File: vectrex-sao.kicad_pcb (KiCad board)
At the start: 2 copper layers, 0 parts

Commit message: initial commit
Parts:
- added C1-1: LED0603_NOOUTLINE, Capacitor_SMD:C_0603_1608Metric, F.Cu at (112.6, 42.4)
- added C1-2: LED0603_NOOUTLINE, Capacitor_SMD:C_0603_1608Metric, F.Cu at (121.6, 49.9)
- added C1-3: LED0603_NOOUTLINE, Capacitor_SMD:C_0603_1608Metric, F.Cu at (91.7, 57.5)
- added C1-4: LED0603_NOOUTLINE, Capacitor_SMD:C_0603_1608Metric, F.Cu at (100.6, 34.9)
- added C1-5: LED0603_NOOUTLINE, Capacitor_SMD:C_0603_1608Metric, F.Cu at (103.7, 57.4)
- added C1-6: LED0603_NOOUTLINE, Capacitor_SMD:C_0603_1608Metric, F.Cu at (128.7, 29.8)
- added C1-7: LED0603_NOOUTLINE, Capacitor_SMD:C_0603_1608Metric, F.Cu at (136.7, 29.8)
- added C2-1: LED0603_NOOUTLINE, Capacitor_SMD:C_0603_1608Metric, F.Cu at (100.6, 32.3)
- added C2-2: LED0603_NOOUTLINE, Capacitor_SMD:C_0603_1608Metric, F.Cu at (108.6, 29.8)
- added C2-3: LED0603_NOOUTLINE, Capacitor_SMD:C_0603_1608Metric, F.Cu at (87.7, 57.5)
- added C2-4: LED0603_NOOUTLINE, Capacitor_SMD:C_0603_1608Metric, F.Cu at (112.6, 44.9)
- added C2-5: LED0603_NOOUTLINE, Capacitor_SMD:C_0603_1608Metric, F.Cu at (125.6, 47.4)
- added C2-6: LED0603_NOOUTLINE, Capacitor_SMD:C_0603_1608Metric, F.Cu at (101.6, 47.4)
- added C2-7: LED0603_NOOUTLINE, Capacitor_SMD:C_0603_1608Metric, F.Cu at (108.6, 42.4)
- added C3-1: LED0603_NOOUTLINE, Capacitor_SMD:C_0603_1608Metric, F.Cu at (100.6, 44.9)
- added C3-2: LED0603_NOOUTLINE, Capacitor_SMD:C_0603_1608Metric, F.Cu at (108.6, 34.9)
- added C3-3: LED0603_NOOUTLINE, Capacitor_SMD:C_0603_1608Metric, F.Cu at (104.6, 29.8)
- added C3-4: LED0603_NOOUTLINE, Capacitor_SMD:C_0603_1608Metric, F.Cu at (108.6, 32.3)
- added C3-5: LED0603_NOOUTLINE, Capacitor_SMD:C_0603_1608Metric, F.Cu at (104.6, 34.9)
- added C3-6: LED0603_NOOUTLINE, Capacitor_SMD:C_0603_1608Metric, F.Cu at (120.7, 37.4)
- added C3-7: LED0603_NOOUTLINE, Capacitor_SMD:C_0603_1608Metric, F.Cu at (101.6, 49.9)
- added C4-1: LED0603_NOOUTLINE, Capacitor_SMD:C_0603_1608Metric, F.Cu at (101.6, 52.4)
- added C4-2: LED0603_NOOUTLINE, Capacitor_SMD:C_0603_1608Metric, F.Cu at (112.6, 29.8)
- added C4-3: LED0603_NOOUTLINE, Capacitor_SMD:C_0603_1608Metric, F.Cu at (113.6, 47.4)
- added C4-4: LED0603_NOOUTLINE, Capacitor_SMD:C_0603_1608Metric, F.Cu at (111.8, 57.4)
- added C4-5: LED0603_NOOUTLINE, Capacitor_SMD:C_0603_1608Metric, F.Cu at (124.7, 37.4)
- added C4-6: LED0603_NOOUTLINE, Capacitor_SMD:C_0603_1608Metric, F.Cu at (128.7, 34.9)
- added C4-7: LED0603_NOOUTLINE, Capacitor_SMD:C_0603_1608Metric, F.Cu at (132.7, 34.9)
- added C5-1: LED0603_NOOUTLINE, Capacitor_SMD:C_0603_1608Metric, F.Cu at (121.6, 47.4)
- added C5-2: LED0603_NOOUTLINE, Capacitor_SMD:C_0603_1608Metric, F.Cu at (117.6, 47.4)
- added C5-3: LED0603_NOOUTLINE, Capacitor_SMD:C_0603_1608Metric, F.Cu at (116.7, 29.8)
- added C5-4: LED0603_NOOUTLINE, Capacitor_SMD:C_0603_1608Metric, F.Cu at (136.7, 34.9)
- added C5-5: LED0603_NOOUTLINE, Capacitor_SMD:C_0603_1608Metric, F.Cu at (99.7, 59.3)
- added C5-6: LED0603_NOOUTLINE, Capacitor_SMD:C_0603_1608Metric, F.Cu at (132.7, 37.4)
- added C5-7: LED0603_NOOUTLINE, Capacitor_SMD:C_0603_1608Metric, F.Cu at (109.6, 52.4)
- added C6-1: LED0603_NOOUTLINE, Capacitor_SMD:C_0603_1608Metric, F.Cu at (107.8, 60.0)
- added C6-2: LED0603_NOOUTLINE, Capacitor_SMD:C_0603_1608Metric, F.Cu at (107.8, 57.4)
- added C6-3: LED0603_NOOUTLINE, Capacitor_SMD:C_0603_1608Metric, F.Cu at (109.6, 47.4)
- added C6-4: LED0603_NOOUTLINE, Capacitor_SMD:C_0603_1608Metric, F.Cu at (128.7, 37.4)
- added C6-5: LED0603_NOOUTLINE, Capacitor_SMD:C_0603_1608Metric, F.Cu at (128.7, 32.3)
- added C6-6: LED0603_NOOUTLINE, Capacitor_SMD:C_0603_1608Metric, F.Cu at (124.7, 39.9)
- added C6-7: LED0603_NOOUTLINE, Capacitor_SMD:C_0603_1608Metric, F.Cu at (136.7, 32.3)
- added C7-1: LED0603_NOOUTLINE, Capacitor_SMD:C_0603_1608Metric, F.Cu at (111.8, 60.0)
- added C7-10: LED0603_NOOUTLINE, Capacitor_SMD:C_0603_1608Metric, F.Cu at (136.7, 37.4)
- added C7-11: LED0603_NOOUTLINE, Capacitor_SMD:C_0603_1608Metric, F.Cu at (105.6, 52.4)
- added C7-12: LED0603_NOOUTLINE, Capacitor_SMD:C_0603_1608Metric, F.Cu at (112.6, 37.4)
- added C7-13: LED0603_NOOUTLINE, Capacitor_SMD:C_0603_1608Metric, F.Cu at (117.6, 49.9)
- added C7-14: LED0603_NOOUTLINE, Capacitor_SMD:C_0603_1608Metric, F.Cu at (120.7, 32.3)
- added C7-2: LED0603_NOOUTLINE, Capacitor_SMD:C_0603_1608Metric, F.Cu at (105.6, 47.4)
- added C7-3: LED0603_NOOUTLINE, Capacitor_SMD:C_0603_1608Metric, F.Cu at (120.7, 44.9)
- added C7-4: LED0603_NOOUTLINE, Capacitor_SMD:C_0603_1608Metric, F.Cu at (115.8, 54.9)
- added C7-5: LED0603_NOOUTLINE, Capacitor_SMD:C_0603_1608Metric, F.Cu at (108.6, 39.9)
- added C7-6: LED0603_NOOUTLINE, Capacitor_SMD:C_0603_1608Metric, F.Cu at (132.7, 29.8)
- added C7-7: LED0603_NOOUTLINE, Capacitor_SMD:C_0603_1608Metric, F.Cu at (120.7, 42.4)
- added C7-8: LED0603_NOOUTLINE, Capacitor_SMD:C_0603_1608Metric, F.Cu at (117.6, 52.4)
- added C7-9: LED0603_NOOUTLINE, Capacitor_SMD:C_0603_1608Metric, F.Cu at (120.7, 29.8)
- added C8-1: LED0603_NOOUTLINE, Capacitor_SMD:C_0603_1608Metric, F.Cu at (124.7, 44.9)
- added C8-10: LED0603_NOOUTLINE, Capacitor_SMD:C_0603_1608Metric, F.Cu at (128.7, 39.9)
- added C8-11: LED0603_NOOUTLINE, Capacitor_SMD:C_0603_1608Metric, F.Cu at (128.7, 42.4)
- added C8-12: LED0603_NOOUTLINE, Capacitor_SMD:C_0603_1608Metric, F.Cu at (116.7, 44.9)
- added C8-13: LED0603_NOOUTLINE, Capacitor_SMD:C_0603_1608Metric, F.Cu at (124.7, 42.4)
- added C8-14: LED0603_NOOUTLINE, Capacitor_SMD:C_0603_1608Metric, F.Cu at (103.7, 60.0)
- added C8-2: LED0603_NOOUTLINE, Capacitor_SMD:C_0603_1608Metric, F.Cu at (97.6, 51.8)
- added C8-3: LED0603_NOOUTLINE, Capacitor_SMD:C_0603_1608Metric, F.Cu at (132.7, 39.9)
- added C8-4: LED0603_NOOUTLINE, Capacitor_SMD:C_0603_1608Metric, F.Cu at (97.6, 49.3)
- added C8-5: LED0603_NOOUTLINE, Capacitor_SMD:C_0603_1608Metric, F.Cu at (140.7, 32.3)
- added C8-6: LED0603_NOOUTLINE, Capacitor_SMD:C_0603_1608Metric, F.Cu at (132.7, 32.3)
- added C8-7: LED0603_NOOUTLINE, Capacitor_SMD:C_0603_1608Metric, F.Cu at (112.6, 39.9)
- added C8-8: LED0603_NOOUTLINE, Capacitor_SMD:C_0603_1608Metric, F.Cu at (104.6, 37.4)
- added C8-9: LED0603_NOOUTLINE, Capacitor_SMD:C_0603_1608Metric, F.Cu at (100.6, 42.4)
- added U1: PIC16F886-IP, Package_SO:SOIC-28W_7.5x17.9mm_P1.27mm, F.Cu at (77.4, 27.2)
- added U3: NCP1117-3.3_SOT223, Package_TO_SOT_SMD:SOT-223-3_TabPin2, F.Cu at (77.0, 41.7)

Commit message: 4 hours of work redone in 1 hour
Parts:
- removed U3: NCP1117-3.3_SOT223, Package_TO_SOT_SMD:SOT-223-3_TabPin2
- added C1: 10uF, Capacitor_SMD:C_0805_2012Metric, F.Cu at (73.7, 48.3)
- added C2: 10uF, Capacitor_SMD:C_0805_2012Metric, F.Cu at (68.6, 61.0)
- added C3: 0.1uF, Capacitor_SMD:C_0805_2012Metric, F.Cu at (73.7, 53.3)
- added J2: Badgelife_sao_connector_v169bis, vectrex-sao:Badgelife-SAOv169-SAO-2x3, F.Cu at (86.4, 58.4)
- added R1: 10K, vectrex-sao:R_Array_Convex_4x0603_CAT16-F4, F.Cu at (68.6, 53.3)
- added SJ1: SOLDERJUMPER, vectrex-sao:SolderJumper-2_P1.3mm_Open_RoundedPad1.0x1.5mm, F.Cu at (73.7, 61.0)
- added U2: IS31FL3731-SALS2, Package_DFN_QFN:QFN-28-1EP_4x4mm_P0.4mm_EP2.3x2.3mm, F.Cu at (71.1, 17.8)
- C1-1, C1-2, C1-3, C1-4, C1-5, C1-6, C1-7, C2-1, C2-2, C2-3, C2-4, C2-5, C2-6, C2-7, C3-1, C3-2, C3-3, C3-4, C3-5, C3-6, C3-7, C4-1, C4-2, C4-3, C4-4, C4-5, C4-6, C4-7, C5-1, C5-2, C5-3, C5-4, C5-5, C5-6, C5-7, C6-1, C6-2, C6-3, C6-4, C6-5, C6-6, C6-7, C7-1, C7-10, C7-11, C7-12, C7-13, C7-14, C7-2, C7-3, C7-4, C7-5, C7-6, C7-7, C7-8, C7-9, C8-1, C8-10, C8-11, C8-12, C8-13, C8-14, C8-2, C8-3, C8-4, C8-5, C8-6, C8-7, C8-8, C8-9: footprint Capacitor_SMD:C_0603_1608Metric -> vectrex-sao:C_0603_1608Metric
- moved C7-10 50.7 mm to (86.4, 43.2), turned to -135 degrees
- moved C8-5 49.6 mm to (91.4, 38.1), turned to 45 degrees
- moved C5-4 48.0 mm to (88.9, 30.5), turned to 45 degrees
- moved C1-2 48.0 mm to (83.8, 20.3), turned to 45 degrees
- moved C8-3 46.4 mm to (86.4, 38.1), turned to 45 degrees
- moved C8-1 43.9 mm to (81.3, 38.1), turned to 45 degrees
- moved C5-1 43.7 mm to (81.3, 30.5), turned to 45 degrees
- moved C8-10 42.3 mm to (86.4, 40.6), turned to -135 degrees
- moved C2-5 42.1 mm to (91.4, 22.9), turned to 45 degrees
- moved C1-7 41.3 mm to (96.5, 20.3), turned to 45 degrees
- moved C6-7 40.2 mm to (96.5, 33.0), turned to 45 degrees
- moved C6-4 40.0 mm to (88.9, 33.0), turned to 45 degrees
- moved C8-11 39.8 mm to (88.9, 40.6), turned to -135 degrees
- moved C5-6 39.3 mm to (94.0, 30.5), turned to 45 degrees
- moved C7-9 39.2 mm to (83.8, 43.2), turned to -135 degrees
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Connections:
- C1-1 pad 1: (no net) -> /CA1
- C1-1 pad 2: (no net) -> /CA3
- C1-2 pad 1: (no net) -> /CA1
- C1-2 pad 2: (no net) -> /CA4
- C1-3 pad 1: (no net) -> /CA1
- C1-3 pad 2: (no net) -> /CA5
- C1-4 pad 1: (no net) -> /CA1
- C1-4 pad 2: (no net) -> /CA6
- C1-5 pad 1: (no net) -> /CA1
- C1-5 pad 2: (no net) -> /CA7
- C1-6 pad 1: (no net) -> /CA1
- C1-6 pad 2: (no net) -> /CA8
- C1-7 pad 1: (no net) -> /CA1
- C1-7 pad 2: (no net) -> /CA9
- C2-1 pad 1: (no net) -> /CA2
- C2-1 pad 2: (no net) -> /CA3
- C2-2 pad 1: (no net) -> /CA2
- C2-2 pad 2: (no net) -> /CA4
- C2-3 pad 1: (no net) -> /CA2
- C2-3 pad 2: (no net) -> /CA5
- C2-4 pad 1: (no net) -> /CA2
- C2-4 pad 2: (no net) -> /CA6
- C2-5 pad 1: (no net) -> /CA2
- C2-5 pad 2: (no net) -> /CA7
- C2-6 pad 1: (no net) -> /CA2
- C2-6 pad 2: (no net) -> /CA8
- C2-7 pad 1: (no net) -> /CA2
- C2-7 pad 2: (no net) -> /CA9
- C3-1 pad 1: (no net) -> /CA3
- C3-1 pad 2: (no net) -> /CA2
- C3-2 pad 1: (no net) -> /CA3
- C3-2 pad 2: (no net) -> /CA4
- C3-3 pad 1: (no net) -> /CA3
- C3-3 pad 2: (no net) -> /CA5
- C3-4 pad 1: (no net) -> /CA3
- C3-4 pad 2: (no net) -> /CA6
- C3-5 pad 1: (no net) -> /CA3
- C3-5 pad 2: (no net) -> /CA7
- C3-6 pad 1: (no net) -> /CA3
- C3-6 pad 2: (no net) -> /CA8
- C3-7 pad 1: (no net) -> /CA3
- C3-7 pad 2: (no net) -> /CA9
- C4-1 pad 1: (no net) -> /CA4
- C4-1 pad 2: (no net) -> /CA2
- C4-2 pad 1: (no net) -> /CA4
- C4-2 pad 2: (no net) -> /CA3
- C4-3 pad 1: (no net) -> /CA4
- C4-3 pad 2: (no net) -> /CA5
- C4-4 pad 1: (no net) -> /CA4
- C4-4 pad 2: (no net) -> /CA6
- C4-5 pad 1: (no net) -> /CA4
- C4-5 pad 2: (no net) -> /CA7
- C4-6 pad 1: (no net) -> /CA4
- C4-6 pad 2: (no net) -> /CA8
- C4-7 pad 1: (no net) -> /CA4
- C4-7 pad 2: (no net) -> /CA9
- C5-1 pad 1: (no net) -> /CA5
- C5-1 pad 2: (no net) -> /CA2
- C5-2 pad 1: (no net) -> /CA5
- C5-2 pad 2: (no net) -> /CA3
- C5-3 pad 1: (no net) -> /CA5
- C5-3 pad 2: (no net) -> /CA4
- C5-4 pad 1: (no net) -> /CA5
- C5-4 pad 2: (no net) -> /CA6
- C5-5 pad 1: (no net) -> /CA5
- C5-5 pad 2: (no net) -> /CA7
- C5-6 pad 1: (no net) -> /CA5
- C5-6 pad 2: (no net) -> /CA8
- C5-7 pad 1: (no net) -> /CA5
- C5-7 pad 2: (no net) -> /CA9
- C6-1 pad 1: (no net) -> /CA6
- C6-1 pad 2: (no net) -> /CA2
- C6-2 pad 1: (no net) -> /CA6
- C6-2 pad 2: (no net) -> /CA3
- C6-3 pad 1: (no net) -> /CA6
- C6-3 pad 2: (no net) -> /CA4
- C6-4 pad 1: (no net) -> /CA6
- C6-4 pad 2: (no net) -> /CA5
- C6-5 pad 1: (no net) -> /CA6
- C6-5 pad 2: (no net) -> /CA7
- C6-6 pad 1: (no net) -> /CA6
- C6-6 pad 2: (no net) -> /CA8
- C6-7 pad 1: (no net) -> /CA6
- C6-7 pad 2: (no net) -> /CA9
- C7-1 pad 1: (no net) -> /CA7
- C7-1 pad 2: (no net) -> /CA2
- C7-10 pad 1: (no net) -> /CB7
- C7-10 pad 2: (no net) -> /CB3
- C7-11 pad 1: (no net) -> /CB7
- C7-11 pad 2: (no net) -> /CB4
- C7-12 pad 1: (no net) -> /CB7
- C7-12 pad 2: (no net) -> /CB5
- C7-13 pad 1: (no net) -> /CB7
- C7-13 pad 2: (no net) -> /CB6
- C7-14 pad 1: (no net) -> /CB7
- C7-14 pad 2: (no net) -> /CB8
- C7-2 pad 1: (no net) -> /CA7
- C7-2 pad 2: (no net) -> /CA3
- C7-3 pad 1: (no net) -> /CA7
- C7-3 pad 2: (no net) -> /CA4
- C7-4 pad 1: (no net) -> /CA7
- C7-4 pad 2: (no net) -> /CA5
- C7-5 pad 1: (no net) -> /CA7
- C7-5 pad 2: (no net) -> /CA6
- C7-6 pad 1: (no net) -> /CA7
- C7-6 pad 2: (no net) -> /CA8
- C7-7 pad 1: (no net) -> /CA7
- C7-7 pad 2: (no net) -> /CA9
- C7-8 pad 1: (no net) -> /CB7
- C7-8 pad 2: (no net) -> /CB1
- C7-9 pad 1: (no net) -> /CB7
- C7-9 pad 2: (no net) -> /CB2
- C8-1 pad 1: (no net) -> /CA8
- C8-1 pad 2: (no net) -> /CA2
- C8-10 pad 1: (no net) -> /CB8
- C8-10 pad 2: (no net) -> /CB3
- C8-11 pad 1: (no net) -> /CB8
- C8-11 pad 2: (no net) -> /CB4
- C8-12 pad 1: (no net) -> /CB8
- C8-12 pad 2: (no net) -> /CB5
- C8-13 pad 1: (no net) -> /CB8
- C8-13 pad 2: (no net) -> /CB6
- C8-14 pad 1: (no net) -> /CB8
- C8-14 pad 2: (no net) -> /CB7
- C8-2 pad 1: (no net) -> /CA8
- C8-2 pad 2: (no net) -> /CA3
- C8-3 pad 1: (no net) -> /CA8
- C8-3 pad 2: (no net) -> /CA4
- C8-4 pad 1: (no net) -> /CA8
- C8-4 pad 2: (no net) -> /CA5
- C8-5 pad 1: (no net) -> /CA8
- C8-5 pad 2: (no net) -> /CA6
- C8-6 pad 1: (no net) -> /CA8
- C8-6 pad 2: (no net) -> /CA7
- C8-7 pad 1: (no net) -> /CA8
- C8-7 pad 2: (no net) -> /CA9
- C8-8 pad 1: (no net) -> /CB8
- C8-8 pad 2: (no net) -> /CB1
- C8-9 pad 1: (no net) -> /CB8
- C8-9 pad 2: (no net) -> /CB2
- U1 pad 1: unconnected-(U1-Pad1) -> /n_MCLR
- U1 pad 14: unconnected-(U1-Pad14) -> /SCL
- U1 pad 15: unconnected-(U1-Pad15) -> /SDA
- U1 pad 19: unconnected-(U1-Pad19) -> GND
- U1 pad 20: unconnected-(U1-Pad20) -> +3.3V
- U1 pad 27: unconnected-(U1-Pad27) -> /ICSPCLK
- U1 pad 28: unconnected-(U1-Pad28) -> /ICSPDAT
- U1 pad 8: unconnected-(U1-Pad8) -> GND

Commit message: tweaks
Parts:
- moved C2 16.1 mm to (73.7, 45.7)
- moved C1 2.54 mm to (73.7, 50.8)
- moved C3 2.54 mm to (73.7, 55.9)
- moved SJ1 2.54 mm to (73.7, 63.5)
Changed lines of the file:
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@@
   )
   (footprint "vectrex-sao:SolderJumper-2_P1.3mm_Open_RoundedPad1.0x1.5mm" (layer "F.Cu")
-    (at 73.66 60.96)
+    (at 73.66 63.5)
     (descr "SMD Solder Jumper, 1x1.5mm, rounded Pads, 0.3mm gap, open")
     (tags "solder jumper open")
@@
       (effects (font (size 1 1) (thickness 0.15)))
     )
-    (fp_text value "SOLDERJUMPER" (at 0.2 2.4) (layer "F.Fab")
+    (fp_text value "SOLDERJUMPER" (at 0.2 2.4) (layer "F.Fab") hide
       (effects (font (size 1 1) (thickness 0.15)))
     )
@@
   )
   (footprint "Capacitor_SMD:C_0805_2012Metric" (layer "F.Cu")
-    (at 73.66 48.26)
+    (at 73.66 50.8)
     (descr "Capacitor SMD 0805 (2012 Metric), square (rectangular) end terminal, IPC_7351 nominal, (Body size source: IPC-SM-782 page 76, https://www.pcb-3d.com/wordpress/wp-content/uploads/ipc-sm-782a_amendment_1_and_2.pdf, https://docs.google.com/spreadsheets/d/1BsfQQcO9C6DZCsRaXUlFlo91Tg2WpOkGARC1WS5S8t0/edit?usp=sharing), generated with kicad-footprint-generator")
     (tags "capacitor")
@@
       (effects (font (size 1 1) (thickness 0.15)) (justify mirror))
     )
-    (fp_text value "Badgelife_sao_connector_v169bis" (at 0 7.54) (layer "F.Fab")
+    (fp_text value "Badgelife_sao_connector_v169bis" (at 5.08 5.08) (layer "F.Fab") hide
       (effects (font (size 1 1) (thickness 0.15)))
     )
@@
   )
   (footprint "Capacitor_SMD:C_0805_2012Metric" (layer "F.Cu")
-    (at 68.58 60.96)
+    (at 73.66 45.72)
     (descr "Capacitor SMD 0805 (2012 Metric), square (rectangular) end terminal, IPC_7351 nominal, (Body size source: IPC-SM-782 page 76, https://www.pcb-3d.com/wordpress/wp-content/uploads/ipc-sm-782a_amendment_1_and_2.pdf, https://docs.google.com/spreadsheets/d/1BsfQQcO9C6DZCsRaXUlFlo91Tg2WpOkGARC1WS5S8t0/edit?usp=sharing), generated with kicad-footprint-generator")
     (tags "capacitor")
@@
   )
   (footprint "Capacitor_SMD:C_0805_2012Metric" (layer "F.Cu")
-    (at 73.66 53.34)
+    (at 73.66 55.88)
     (descr "Capacitor SMD 0805 (2012 Metric), square (rectangular) end terminal, IPC_7351 nominal, (Body size source: IPC-SM-782 page 76, https://www.pcb-3d.com/wordpress/wp-content/uploads/ipc-sm-782a_amendment_1_and_2.pdf, https://docs.google.com/spreadsheets/d/1BsfQQcO9C6DZCsRaXUlFlo91Tg2WpOkGARC1WS5S8t0/edit?usp=sharing), generated with kicad-footprint-generator")
     (tags "capacitor")

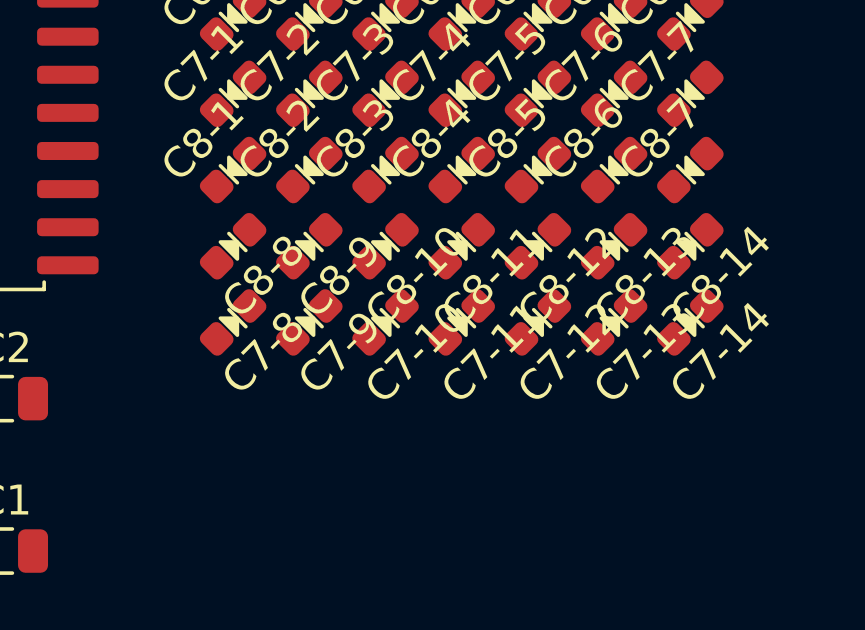
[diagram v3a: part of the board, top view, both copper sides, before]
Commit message: rearrange the bottom two rows
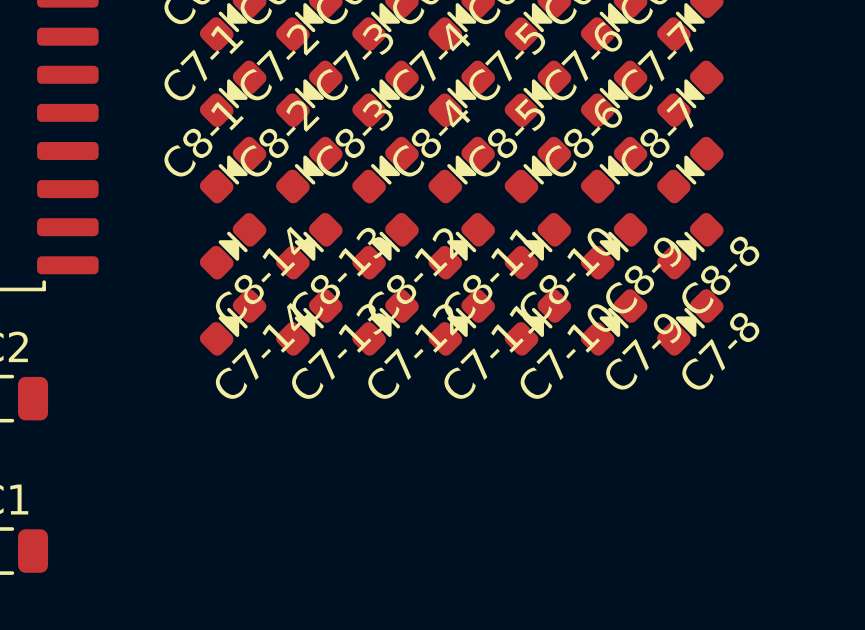
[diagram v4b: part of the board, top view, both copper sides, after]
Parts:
- moved C7-14 15.2 mm to (81.3, 43.2)
- moved C7-8 15.2 mm to (96.5, 43.2)
- moved C8-14 15.2 mm to (81.3, 40.6)
- moved C8-8 15.2 mm to (96.5, 40.6)
- moved C7-13 10.2 mm to (83.8, 43.2)
- moved C7-9 10.2 mm to (94.0, 43.2)
- moved C8-13 10.2 mm to (83.8, 40.6)
- moved C8-9 10.2 mm to (94.0, 40.6)
- moved C7-10 5.08 mm to (91.4, 43.2)
- moved C7-12 5.08 mm to (86.4, 43.2)
- moved C8-10 5.08 mm to (91.4, 40.6)
- moved C8-12 5.08 mm to (86.4, 40.6)
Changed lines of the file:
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@@
   )
   (footprint "vectrex-sao:C_0603_1608Metric" (layer "F.Cu")
-    (at 81.28 43.18 -135)
+    (at 96.52 43.18 -135)
     (descr "Capacitor SMD 0603 (1608 Metric), square (rectangular) end terminal, IPC_7351 nominal, (Body size source: IPC-SM-782 page 76, https://www.pcb-3d.com/wordpress/wp-content/uploads/ipc-sm-782a_amendment_1_and_2.pdf), generated with kicad-footprint-generator")
     (tags "capacitor")
@@
   )
   (footprint "vectrex-sao:C_0603_1608Metric" (layer "F.Cu")
-    (at 83.82 40.64 -135)
+    (at 93.98 40.64 -135)
     (descr "Capacitor SMD 0603 (1608 Metric), square (rectangular) end terminal, IPC_7351 nominal, (Body size source: IPC-SM-782 page 76, https://www.pcb-3d.com/wordpress/wp-content/uploads/ipc-sm-782a_amendment_1_and_2.pdf), generated with kicad-footprint-generator")
     (tags "capacitor")
@@
   )
   (footprint "vectrex-sao:C_0603_1608Metric" (layer "F.Cu")
-    (at 93.98 43.18 -135)
+    (at 83.82 43.18 -135)
     (descr "Capacitor SMD 0603 (1608 Metric), square (rectangular) end terminal, IPC_7351 nominal, (Body size source: IPC-SM-782 page 76, https://www.pcb-3d.com/wordpress/wp-content/uploads/ipc-sm-782a_amendment_1_and_2.pdf), generated with kicad-footprint-generator")
     (tags "capacitor")
@@
   )
   (footprint "vectrex-sao:C_0603_1608Metric" (layer "F.Cu")
-    (at 86.36 40.64 -135)
+    (at 91.44 40.64 -135)
     (descr "Capacitor SMD 0603 (1608 Metric), square (rectangular) end terminal, IPC_7351 nominal, (Body size source: IPC-SM-782 page 76, https://www.pcb-3d.com/wordpress/wp-content/uploads/ipc-sm-782a_amendment_1_and_2.pdf), generated with kicad-footprint-generator")
     (tags "capacitor")
@@
   )
   (footprint "vectrex-sao:C_0603_1608Metric" (layer "F.Cu")
-    (at 96.52 43.18 -135)
+    (at 81.28 43.18 -135)
     (descr "Capacitor SMD 0603 (1608 Metric), square (rectangular) end terminal, IPC_7351 nominal, (Body size source: IPC-SM-782 page 76, https://www.pcb-3d.com/wordpress/wp-content/uploads/ipc-sm-782a_amendment_1_and_2.pdf), generated with kicad-footprint-generator")
     (tags "capacitor")
@@
   )
   (footprint "vectrex-sao:C_0603_1608Metric" (layer "F.Cu")
-    (at 86.36 43.18 -135)
+    (at 91.44 43.18 -135)
     (descr "Capacitor SMD 0603 (1608 Metric), square (rectangular) end terminal, IPC_7351 nominal, (Body size source: IPC-SM-782 page 76, https://www.pcb-3d.com/wordpress/wp-content/uploads/ipc-sm-782a_amendment_1_and_2.pdf), generated with kicad-footprint-generator")
     (tags "capacitor")
@@
   )
   (footprint "vectrex-sao:C_0603_1608Metric" (layer "F.Cu")
-    (at 91.44 43.18 -135)
+    (at 86.36 43.18 -135)
     (descr "Capacitor SMD 0603 (1608 Metric), square (rectangular) end terminal, IPC_7351 nominal, (Body size source: IPC-SM-782 page 76, https://www.pcb-3d.com/wordpress/wp-content/uploads/ipc-sm-782a_amendment_1_and_2.pdf), generated with kicad-footprint-generator")
     (tags "capacitor")
@@
   )
   (footprint "vectrex-sao:C_0603_1608Metric" (layer "F.Cu")
-    (at 96.52 40.64 -135)
+    (at 81.28 40.64 -135)
     (descr "Capacitor SMD 0603 (1608 Metric), square (rectangular) end terminal, IPC_7351 nominal, (Body size source: IPC-SM-782 page 76, https://www.pcb-3d.com/wordpress/wp-content/uploads/ipc-sm-782a_amendment_1_and_2.pdf), generated with kicad-footprint-generator")
     (tags "capacitor")
@@
   )
   (footprint "vectrex-sao:C_0603_1608Metric" (layer "F.Cu")
-    (at 81.28 40.64 -135)
+    (at 96.52 40.64 -135)
     (descr "Capacitor SMD 0603 (1608 Metric), square (rectangular) end terminal, IPC_7351 nominal, (Body size source: IPC-SM-782 page 76, https://www.pcb-3d.com/wordpress/wp-content/uploads/ipc-sm-782a_amendment_1_and_2.pdf), generated with kicad-footprint-generator")
     (tags "capacitor")
@@
   )
   (footprint "vectrex-sao:C_0603_1608Metric" (layer "F.Cu")
-    (at 93.98 40.64 -135)
+    (at 83.82 40.64 -135)
     (descr "Capacitor SMD 0603 (1608 Metric), square (rectangular) end terminal, IPC_7351 nominal, (Body size source: IPC-SM-782 page 76, https://www.pcb-3d.com/wordpress/wp-content/uploads/ipc-sm-782a_amendment_1_and_2.pdf), generated with kicad-footprint-generator")
     (tags "capacitor")
@@
   )
   (footprint "vectrex-sao:C_0603_1608Metric" (layer "F.Cu")
-    (at 83.82 43.18 -135)
+    (at 93.98 43.18 -135)
     (descr "Capacitor SMD 0603 (1608 Metric), square (rectangular) end terminal, IPC_7351 nominal, (Body size source: IPC-SM-782 page 76, https://www.pcb-3d.com/wordpress/wp-content/uploads/ipc-sm-782a_amendment_1_and_2.pdf), generated with kicad-footprint-generator")
     (tags "capacitor")
@@
   )
   (footprint "vectrex-sao:C_0603_1608Metric" (layer "F.Cu")
-    (at 91.44 40.64 -135)
-    (descr "Capacitor SMD 0603 (1608 Metric), square (rectangular) end terminal, IPC_7351 nominal, (Body size source: IPC-SM-782 page 76, https://www.pcb-3d.com/wordpress/wp-content/uploads/ipc-sm-782a_amendment_1_and_2.pdf), generated with kicad-footprint-generator")
-    (tags "capacitor")
+    (at 86.36 40.64 -135)
+    (descr "Capacitor SMD 0603 (1608 Metric), square (rectangular) end terminal, IPC_7351 nominal, (Body size source: IPC-SM-782 page 76, https://www.pcb-3d.com/wordpress/wp-content/uploads/ipc-sm-782a_amendment_1_and_2.pdf), generated with kicad-footprint-generator")
+    (tags "capacitor")
